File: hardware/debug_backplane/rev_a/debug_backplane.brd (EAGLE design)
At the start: 177.8 x 177.8 mm, 296 parts, among them IC3 FT232RQ, J0 BACKPLANE_GENERIC_MODULE_DEBUG, J1 BACKPLANE_GENERIC_MODULE_DEBUG, J2 PJ-102AH, J3 BACKPLANE_CONTROLLER_MODULE, J4 MICRO_USB_B_HIROSE_ZX62-B-5PA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, J5 MICRO_USB_B_HIROSE_ZX62-B-5PA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, J6 MICRO_USB_B_HIROSE_ZX62-B-5PA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, J8 MICRO_USB_B_HIROSE_ZX62-B-5PA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, J9 MICRO_USB_B_HIROSE_ZX62-B-5PA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, Q1 MOSFET-NCHANNELSMD, Q2 MOSFET-NCHANNELSMD, Q3 MOSFET-NCHANNELSMD, Q4 MOSFET-NCHANNELSMD, Q5 MOSFET-NCHANNELSMD, Q6 MOSFET-NCHANNELSMD, Q7 MOSFET-NCHANNELSMD, Q8 MOSFET-NCHANNELSMD, U1 TUSB2077A, U10 SAM4LC8AA, U11 LTC2941, U12 LTC2941, U13 FT232RQ, U14 SN74LVC2T45, U15 SN74LVC2T45, U16 FT232RQ, U2 FXMA2102, U20 TS3USB30E, U21 TS3USB30E, U26 MCP23008, U27 MCP23008, U3 FXMA2102, U4 MAX8887EZK33+T, U40 FT232RQ, U41 FT232RQ, U5 LTC2941, U6 PCA9544AQFN-N20, U7 LTC2941, U8 SN74LVC2T45, U9 SN74LVC2T45, X1 16MHz, Y1 ABMM

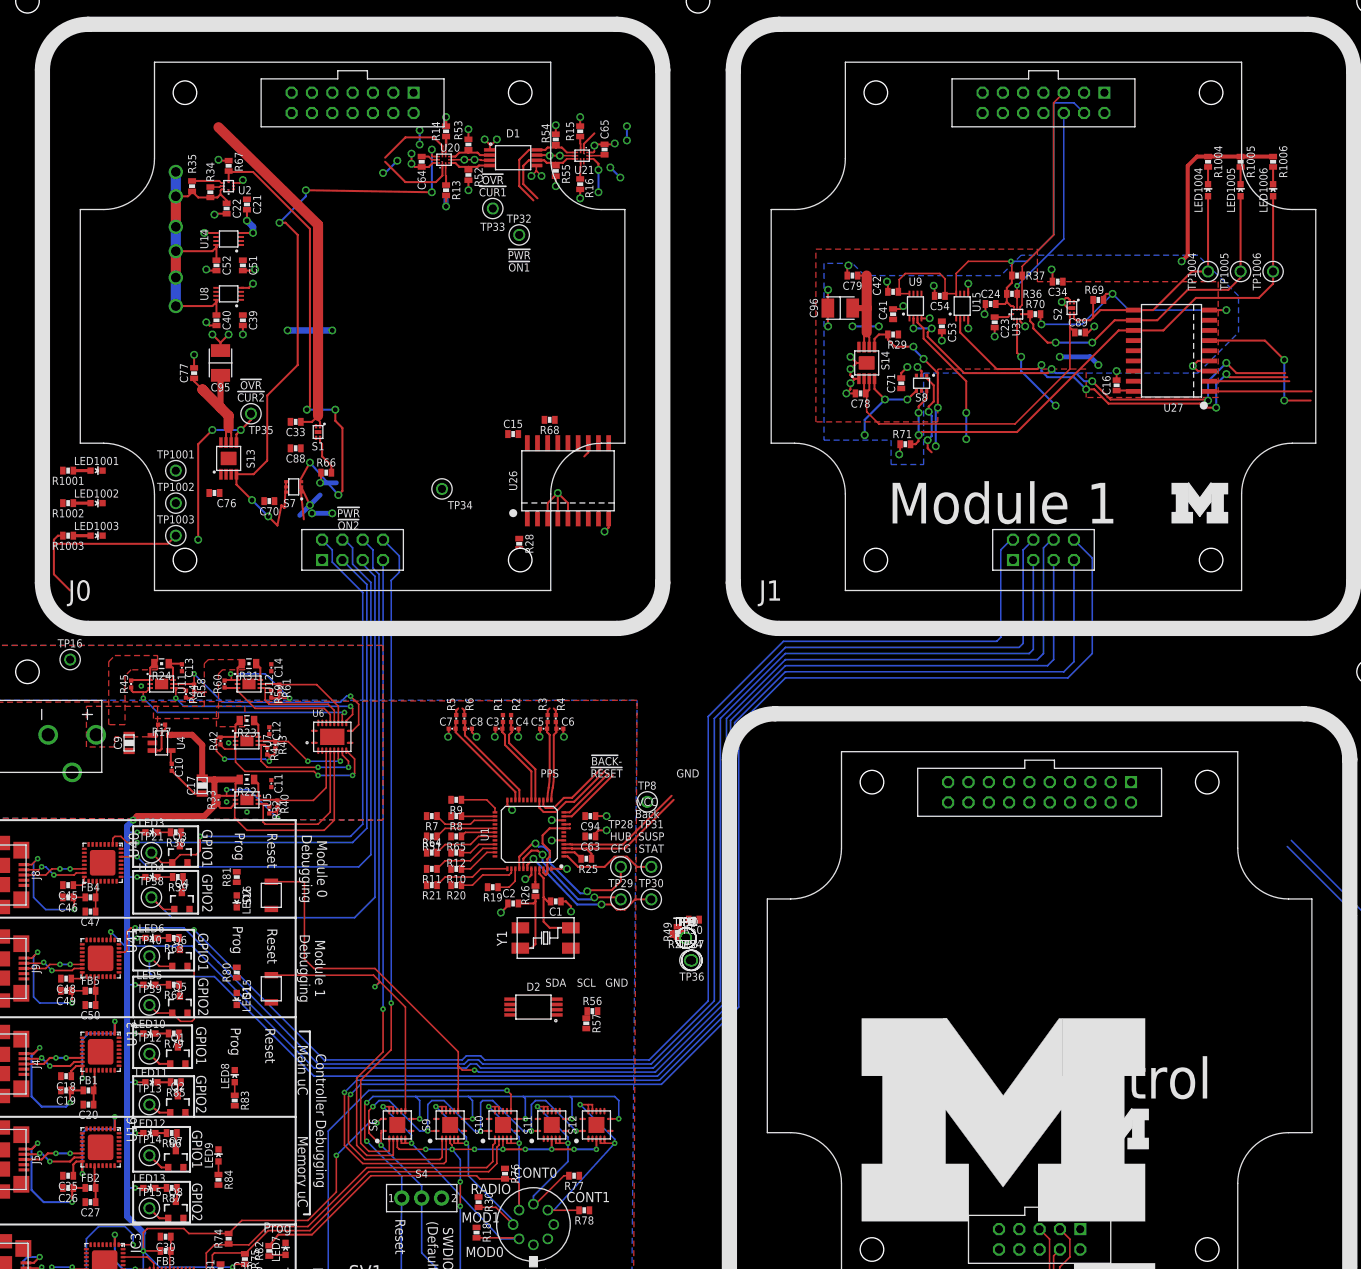
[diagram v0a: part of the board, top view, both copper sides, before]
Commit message: changed mcp23008 to qfn, fixed enabled leds/resistors
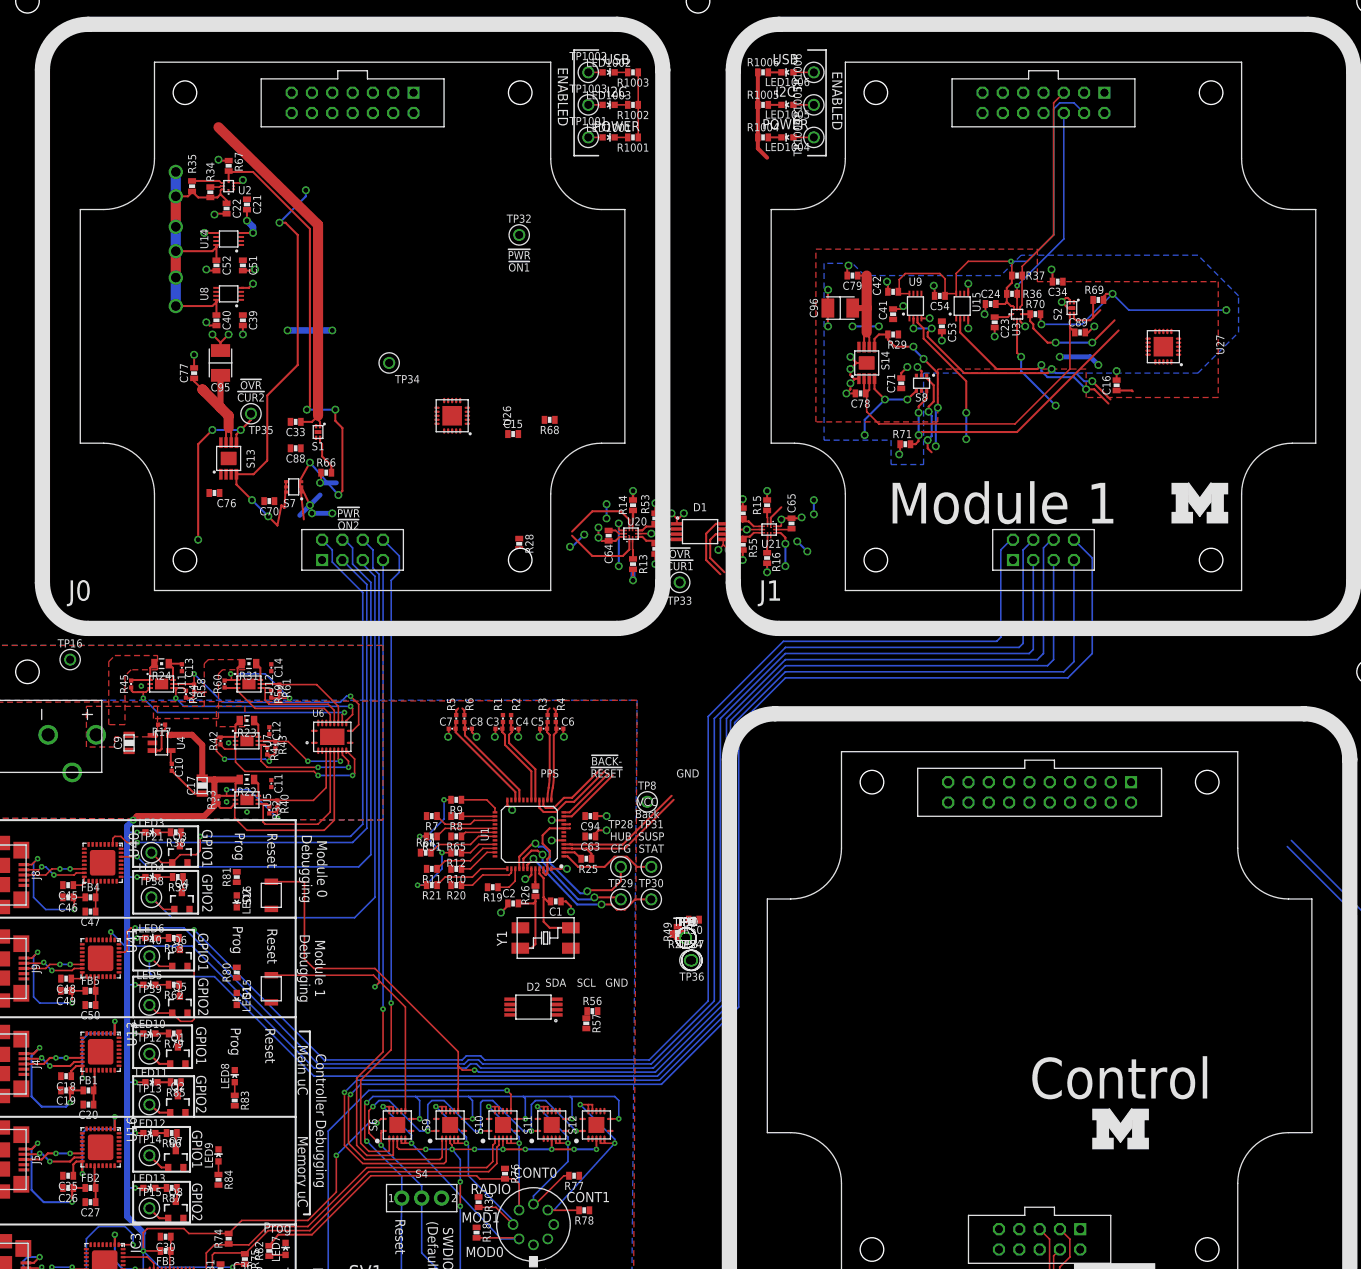
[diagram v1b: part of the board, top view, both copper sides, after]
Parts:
- removed LOGO1: UMICH_SOLID_GIANT, logos:UMICH_SOLID_1000MIL
- R1001, R1002, R1003, R1004, R1005, R1006: value 15Ω -> 1k
- U26, U27: value MCP23008 -> MCP23008QFN; device signpost:SOIC-18 -> signpost:QFN-20-4MM
- moved R1003 91.3 mm to (80.8, 163.8)
- moved R1002 86.4 mm to (80.8, 159.8)
- moved LED1002 83.6 mm to (77.7, 163.8)
- moved LED1003 83.6 mm to (77.7, 159.8)
- moved R1001 82.0 mm to (80.8, 155.7)
- moved LED1001 76.4 mm to (77.7, 155.7)
- moved TP1002 74.6 mm to (75.2, 163.8)
- moved TP1003 74.6 mm to (75.2, 159.8)
- moved TP1001 66.3 mm to (75.2, 155.7)
- moved R1006 64.7 mm to (97.0, 163.8), turned to 0 degrees
- moved TP1006 62.6 mm to (103.4, 163.8)
- moved LED1006 62.5 mm to (100.1, 163.8), turned to 90 degrees
- moved R1005 60.1 mm to (97.0, 159.8), turned to 0 degrees
- moved LED1005 57.6 mm to (100.1, 159.8), turned to 90 degrees
- moved TP1005 57.3 mm to (103.4, 159.8)
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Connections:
- net !BACKPLANE_RESET: now also U26.4, U27.4; no longer U26.6, U27.6
- net GND: now also R1001.1, R1002.1, R1003.1, U26.1, U26.17, U26.2, U26.GND, U27.1, U27.2; no longer LED1001.C, LED1002.C, LED1003.C, U26.4, U26.5, U26.9, U27.3, U27.4
- net MOD0_ISO_I2C: now also LED1002.A, U26.10; no longer R1002.2, U26.11
- net MOD0_ISO_POWER: now also LED1001.A, U26.9; no longer R1001.2, U26.10
- net MOD0_ISO_USB: now also LED1003.A, U26.11; no longer R1003.2, U26.12
- net MOD1_ISO_I2C: now also U27.10; no longer U27.11
- net MOD1_ISO_POWER: now also U27.9; no longer U27.10
- net MOD1_ISO_USB: now also U27.11; no longer U27.12
- net N$1: now also LED1001.C, R1001.2; no longer LED1001.A, R1001.1
- net N$2: now also LED1002.C, R1003.2; no longer LED1002.A, R1002.1
- net N$3: now also LED1003.C, R1002.2; no longer LED1003.A, R1003.1
- net N$33: now also U27.17, U27.GND; no longer U27.9
- net SMBCLK: now also U26.19, U27.19; no longer U26.1, U27.1
- net SMBDATA: now also U26.20, U27.20; no longer U26.2, U27.2
- net VCC_BACKPLANE: now also U27.3; no longer U27.5
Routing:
- net MOD1_ISO_USB: track 71.6 -> 40.9 mm
- net MOD1_ISO_I2C: track 43.8 -> 17.6 mm
- net CONT_MOD1_OUT: track 51.0 -> 24.8 mm, vias 4 -> 2
- net CONT_MOD1_IN: track 57.1 -> 31.3 mm, vias 6 -> 4
- net MOD0_ISO_USB: track 26.2 -> 1.79 mm
- net MOD1_ISO_POWER: track 31.5 -> 9.21 mm
- net GND: track 171.8 -> 150.7 mm, vias 103 -> 99
- net VCC_BACKPLANE: track 46.4 -> 66.2 mm, vias 16 -> 20
- net !BACKPLANE_RESET: track 18.8 -> 0.00 mm, vias 2 -> 0
- net MOD0_USB_!EN: track 80.1 -> 64.4 mm
- net SMBCLK: track 16.4 -> 3.57 mm
- net SMBDATA: track 13.6 -> 3.57 mm
- net N$33: track 32.0 -> 29.8 mm
- net MOD0_ISO_POWER: track 4.94 -> 6.73 mm
- net MOD0_ISO_I2C: track 64.9 -> 66.7 mm
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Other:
- board text added: "ENABLED"
- board text added: "I2C"
- board text added: "POWER"
- board text added: "USB"

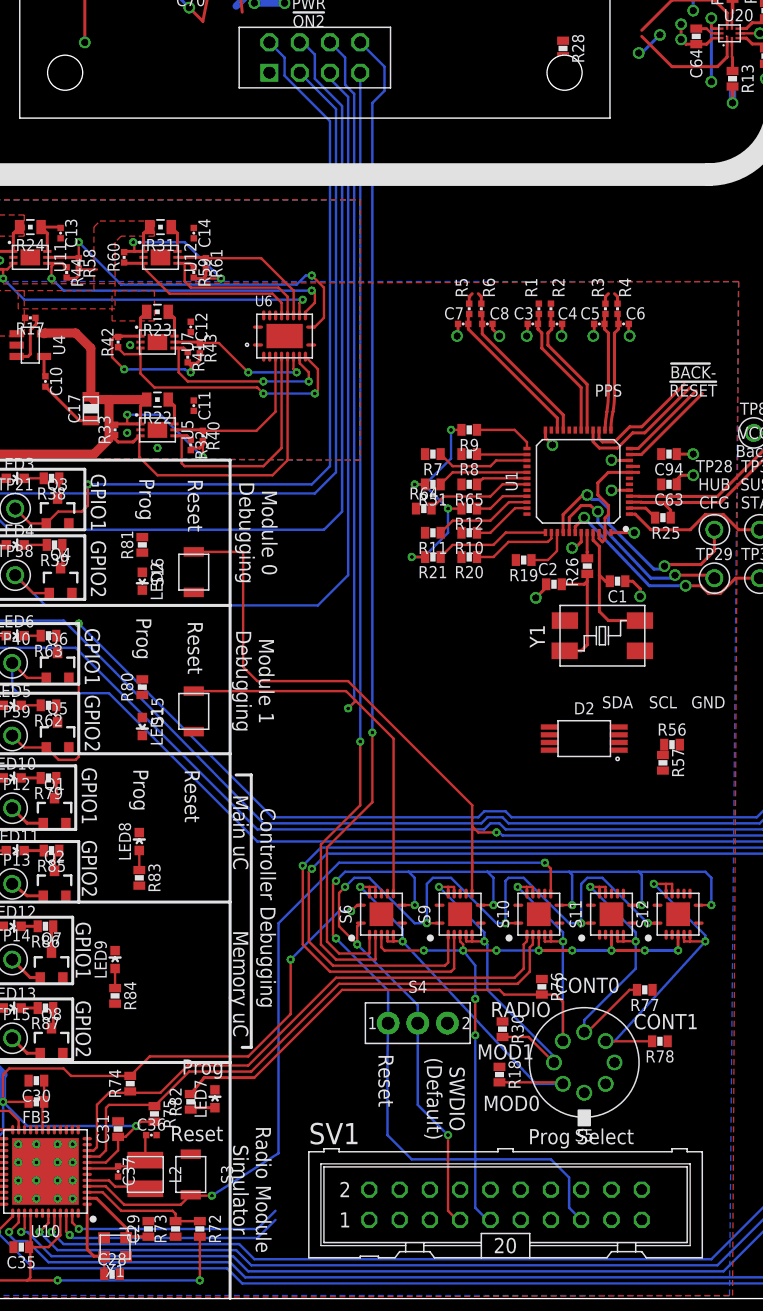
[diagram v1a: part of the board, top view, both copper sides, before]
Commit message: routed usb to radio chip
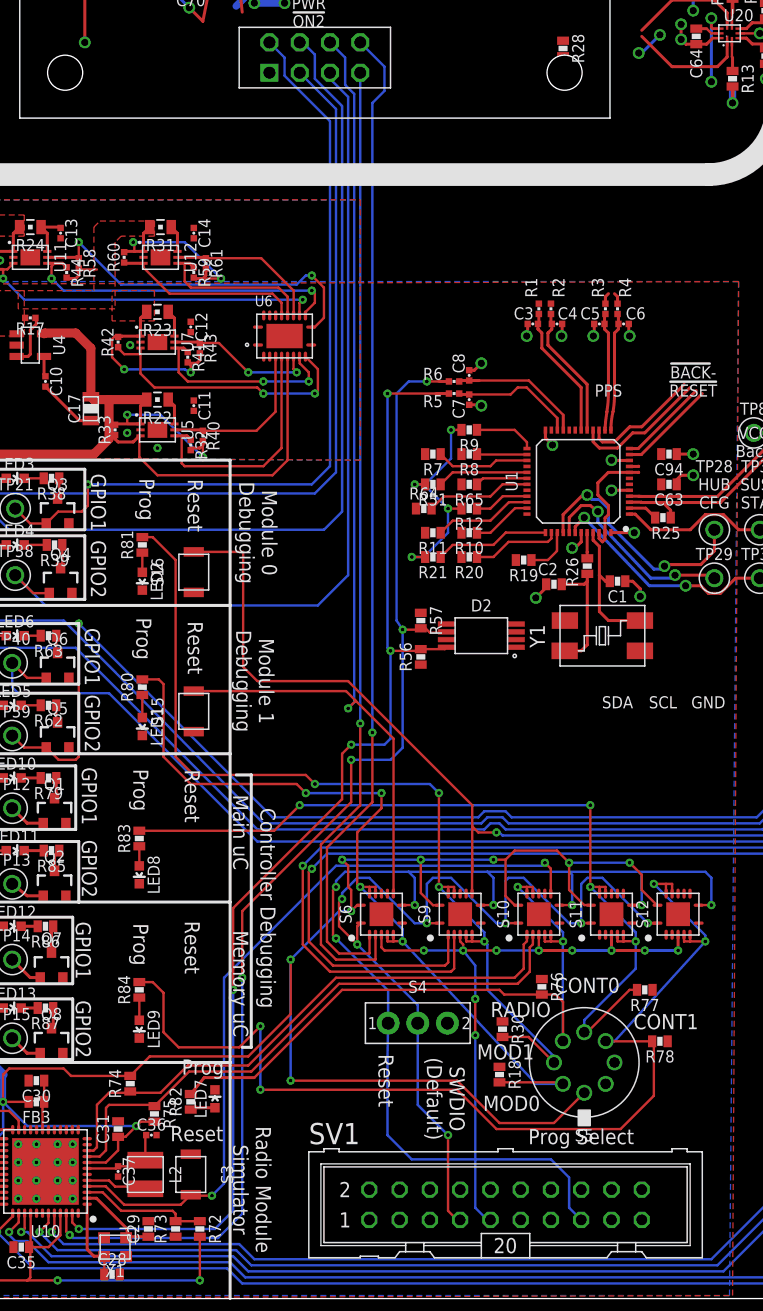
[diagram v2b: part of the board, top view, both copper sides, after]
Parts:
- moved R57 23.6 mm to (54.6, 56.9)
- moved R56 22.3 mm to (54.6, 53.8), turned to 90 degrees
- moved D2 12.2 mm to (59.7, 55.6)
- moved R5 7.22 mm to (57.4, 75.9), turned to 180 degrees
- moved R6 6.51 mm to (57.4, 77.0), turned to 180 degrees
- moved C7 6.37 mm to (58.7, 75.4), turned to 270 degrees
- moved LED9 6.19 mm to (31.0, 22.6), turned to 180 degrees
- moved C8 4.58 mm to (58.7, 77.5), turned to 90 degrees
- moved R83 3.30 mm to (31.0, 38.6), turned to 90 degrees
- moved LED8 2.79 mm to (31.0, 35.6), turned to 180 degrees
- moved R84 2.09 mm to (31.0, 25.9), turned to 90 degrees
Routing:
- net 3V3: track 239.0 -> 324.2 mm, vias 18 -> 24
- net MOD2_USB-: track 20.9 -> 102.6 mm, vias 1 -> 5
- net MOD2_USB+: track 19.6 -> 101.2 mm, vias 1 -> 5
- net PROG4_EN: track 28.7 -> 89.3 mm, vias 2 -> 4
- net PROG1_EN: track 29.0 -> 80.3 mm, vias 2 -> 4
- net PROG3_EN: track 26.3 -> 71.9 mm, vias 2 -> 4
- net PROG0_EN: track 34.9 -> 71.3 mm, vias 2 -> 4
- net HUB_DP3: track 12.9 -> 10.6 mm
- net N$58: track 0.00 -> 1.90 mm
- net N$28: track 0.00 -> 1.65 mm
- net HUB_DM3: track 12.6 -> 11.2 mm
- net RADIO_!RESET: track 64.7 -> 64.0 mm
